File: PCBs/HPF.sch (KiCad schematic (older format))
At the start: 9 parts, among them J5 MEASURE, J7 MEASURE

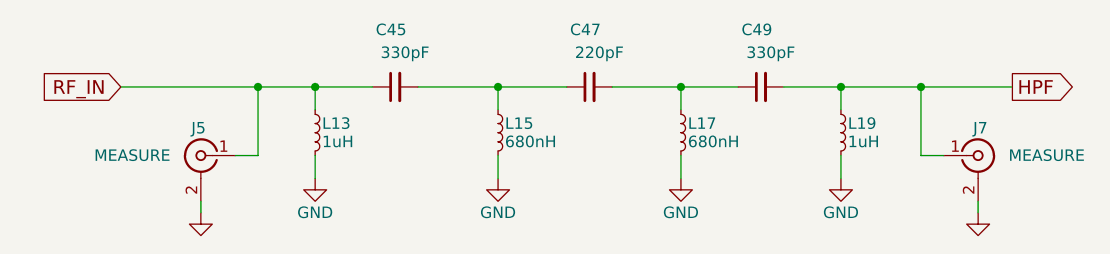
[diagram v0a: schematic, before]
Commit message: ADX988 CAT: add FE, FI commands
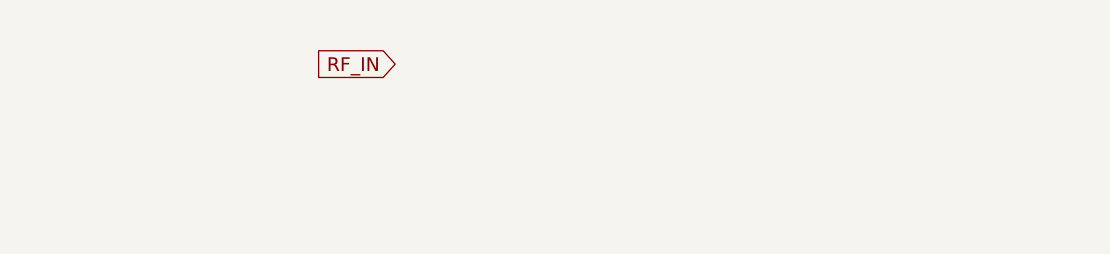
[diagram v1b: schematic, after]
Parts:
- removed C45, C49: 330pF, LCSDR:C_1206_0603, symbol C_Small
- removed C47: 220pF, LCSDR:C_1206_0603, symbol C_Small
- removed J5, J7: MEASURE, LCSDR:U.FL_Molex_MCRF_73412-0110_Vertical, symbol Conn_Coaxial
- removed L13, L19: 1uH, Choke_Axial_ThroughHole:Choke_Horizontal_RM10mm, symbol L_Small
- removed L15: 680nH, Resistors_THT:R_Axial_DIN0309_L9.0mm_D3.2mm_P2.54mm_Vertical, symbol L_Small
- removed L17: 680nH, Choke_Axial_ThroughHole:Choke_Horizontal_RM10mm, symbol L_Small
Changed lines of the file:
@@
 Comment4 ""
 $EndDescr
-$Comp
-L C_Small C45
-U 1 1 630A3609
-P 3700 2200
-F 0 "C45" V 3950 2150 50  0000 L CNN
-F 1 "330pF" V 3850 2050 50  0000 L CNN
-F 2 "LCSDR:C_1206_0603" H 3700 2200 50  0001 C CNN
-F 3 "" H 3700 2200 50  0001 C CNN
-	1    3700 2200
-	0    -1   -1   0
-$EndComp
-$Comp
-L C_Small C47
-U 1 1 630A3651
-P 4550 2200
-F 0 "C47" V 4800 2150 50  0000 L CNN
-F 1 "220pF" V 4700 2050 50  0000 L CNN
-F 2 "LCSDR:C_1206_0603" H 4550 2200 50  0001 C CNN
-F 3 "" H 4550 2200 50  0001 C CNN
-	1    4550 2200
-	0    -1   -1   0
-$EndComp
-$Comp
-L C_Small C49
-U 1 1 630A366B
-P 5300 2200
-F 0 "C49" V 5550 2150 50  0000 L CNN
-F 1 "330pF" V 5450 2050 50  0000 L CNN
-F 2 "LCSDR:C_1206_0603" H 5300 2200 50  0001 C CNN
-F 3 "" H 5300 2200 50  0001 C CNN
-	1    5300 2200
-	0    -1   -1   0
-$EndComp
-$Comp
-L L_Small L17
-U 1 1 630A36DA
-P 4950 2400
-F 0 "L17" H 4980 2440 50  0000 L CNN
-F 1 "680nH" H 4980 2360 50  0000 L CNN
-F 2 "Choke_Axial_ThroughHole:Choke_Horizontal_RM10mm" H 4950 2400 50  0001 C CNN
-F 3 "" H 4950 2400 50  0001 C CNN
-	1    4950 2400
-	1    0    0    -1
-$EndComp
-$Comp
-L L_Small L19
-U 1 1 630A370D
-P 5650 2400
-F 0 "L19" H 5680 2440 50  0000 L CNN
-F 1 "1uH" H 5680 2360 50  0000 L CNN
-F 2 "Choke_Axial_ThroughHole:Choke_Horizontal_RM10mm" H 5650 2400 50  0001 C CNN
-F 3 "" H 5650 2400 50  0001 C CNN
-	1    5650 2400
-	1    0    0    -1
-$EndComp
-$Comp
-L L_Small L15
-U 1 1 630A3742
-P 4150 2400
-F 0 "L15" H 4180 2440 50  0000 L CNN
-F 1 "680nH" H 4180 2360 50  0000 L CNN
-F 2 "Resistors_THT:R_Axial_DIN0309_L9.0mm_D3.2mm_P2.54mm_Vertical" H 4150 2400 50  0001 C CNN
-F 3 "" H 4150 2400 50  0001 C CNN
-	1    4150 2400
-	1    0    0    -1
-$EndComp
-$Comp
-L L_Small L13
-U 1 1 630A3786
-P 3350 2400
-F 0 "L13" H 3380 2440 50  0000 L CNN
-F 1 "1uH" H 3380 2360 50  0000 L CNN
-F 2 "Choke_Axial_ThroughHole:Choke_Horizontal_RM10mm" H 3350 2400 50  0001 C CNN
-F 3 "" H 3350 2400 50  0001 C CNN
-	1    3350 2400
-	1    0    0    -1
-$EndComp
-$Comp
-L GND #PWR096
-U 1 1 630A3912
-P 5650 2600
-F 0 "#PWR096" H 5650 2350 50  0001 C CNN
-F 1 "GND" H 5650 2450 50  0000 C CNN
-F 2 "" H 5650 2600 50  0001 C CNN
-F 3 "" H 5650 2600 50  0001 C CNN
-	1    5650 2600
-	1    0    0    -1
-$EndComp
-$Comp
-L GND #PWR097
-U 1 1 630A3972
-P 4950 2600
-F 0 "#PWR097" H 4950 2350 50  0001 C CNN
-F 1 "GND" H 4950 2450 50  0000 C CNN
-F 2 "" H 4950 2600 50  0001 C CNN
-F 3 "" H 4950 2600 50  0001 C CNN
-	1    4950 2600
-	1    0    0    -1
-$EndComp
-$Comp
-L GND #PWR098
-U 1 1 630A39B4
-P 4150 2600
-F 0 "#PWR098" H 4150 2350 50  0001 C CNN
-F 1 "GND" H 4150 2450 50  0000 C CNN
-F 2 "" H 4150 2600 50  0001 C CNN
-F 3 "" H 4150 2600 50  0001 C CNN
-	1    4150 2600
-	1    0    0    -1
-$EndComp
-$Comp
-L GND #PWR099
-U 1 1 630A39EF
-P 3350 2600
-F 0 "#PWR099" H 3350 2350 50  0001 C CNN
-F 1 "GND" H 3350 2450 50  0000 C CNN
-F 2 "" H 3350 2600 50  0001 C CNN
-F 3 "" H 3350 2600 50  0001 C CNN
-	1    3350 2600
-	1    0    0    -1
-$EndComp
-Wire Wire Line
-	4650 2200 5200 2200
-Wire Wire Line
-	4950 2300 4950 2200
-Connection ~ 4950 2200
-Wire Wire Line
-	5400 2200 6400 2200
-Wire Wire Line
-	5650 2200 5650 2300
-Wire Wire Line
-	3800 2200 4450 2200
-Wire Wire Line
-	4150 2200 4150 2300
-Connection ~ 4150 2200
-Wire Wire Line
-	2500 2200 3600 2200
-Wire Wire Line
-	3350 2200 3350 2300
-Connection ~ 5650 2200
-Connection ~ 3350 2200
-Wire Wire Line
-	5650 2500 5650 2600
-Wire Wire Line
-	4950 2500 4950 2600
-Wire Wire Line
-	4150 2500 4150 2600
-Wire Wire Line
-	3350 2600 3350 2500
-Text GLabel 2500 2200 0    60   Input ~ 0
+Text GLabel 3700 2100 0    60   Input ~ 0
 RF_IN
-Text GLabel 6400 2200 2    60   Output ~ 0
-HPF
-$Comp
-L Conn_Coaxial J7
-U 1 1 630C7FBA
-P 6250 2500
-F 0 "J7" H 6260 2620 50  0000 C CNN
-F 1 "MEASURE" H 6550 2500 50  0000 C CNN
-F 2 "LCSDR:U.FL_Molex_MCRF_73412-0110_Vertical" H 6250 2500 50  0001 C CNN
-F 3 "" H 6250 2500 50  0001 C CNN
-	1    6250 2500
-	1    0    0    -1
-$EndComp
-$Comp
-L GND #PWR0100
-U 1 1 630C7FC1
-P 6250 2750
-F 0 "#PWR0100" H 6250 2500 50  0001 C CNN
-F 1 "GND" H 6250 2600 50  0001 C CNN
-F 2 "" H 6250 2750 50  0001 C CNN
-F 3 "" H 6250 2750 50  0001 C CNN
-	1    6250 2750
-	-1   0    0    -1
-$EndComp
-Wire Wire Line
-	6250 2750 6250 2700
-Wire Wire Line
-	6100 2500 6000 2500
-Wire Wire Line
-	6000 2500 6000 2200
-Connection ~ 6000 2200
-$Comp
-L Conn_Coaxial J5
-U 1 1 630C80F5
-P 2850 2500
-F 0 "J5" H 2860 2620 50  0000 C CNN
-F 1 "MEASURE" H 3150 2500 50  0000 C CNN
-F 2 "LCSDR:U.FL_Molex_MCRF_73412-0110_Vertical" H 2850 2500 50  0001 C CNN
-F 3 "" H 2850 2500 50  0001 C CNN
-	1    2850 2500
-	-1   0    0    -1
-$EndComp
-$Comp
-L GND #PWR0101
-U 1 1 630C80FB
-P 2850 2750
-F 0 "#PWR0101" H 2850 2500 50  0001 C CNN
-F 1 "GND" H 2850 2600 50  0001 C CNN
-F 2 "" H 2850 2750 50  0001 C CNN
-F 3 "" H 2850 2750 50  0001 C CNN
-	1    2850 2750
-	1    0    0    -1
-$EndComp
-Wire Wire Line
-	2850 2750 2850 2700
-Wire Wire Line
-	3000 2500 3100 2500
-Wire Wire Line
-	3100 2500 3100 2200
-Connection ~ 3100 2200
 $EndSCHEMATC
